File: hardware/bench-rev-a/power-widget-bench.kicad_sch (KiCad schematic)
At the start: 0 parts

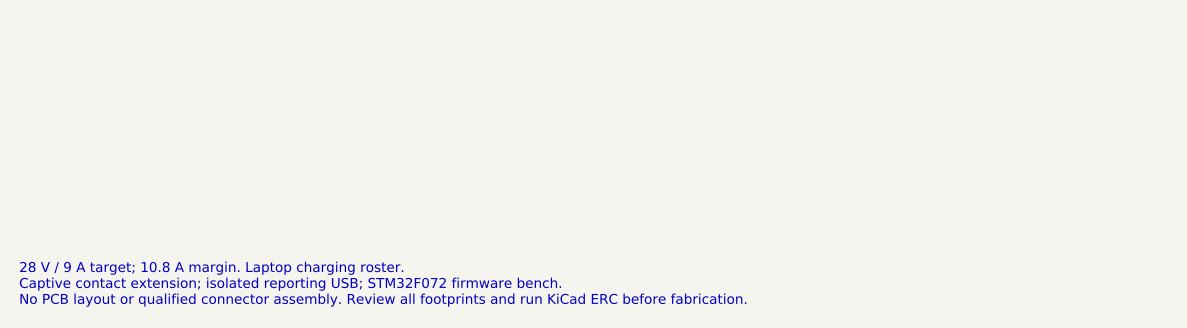
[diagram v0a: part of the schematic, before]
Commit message: Route the firmware bench PCB and record clean native KiCad checks
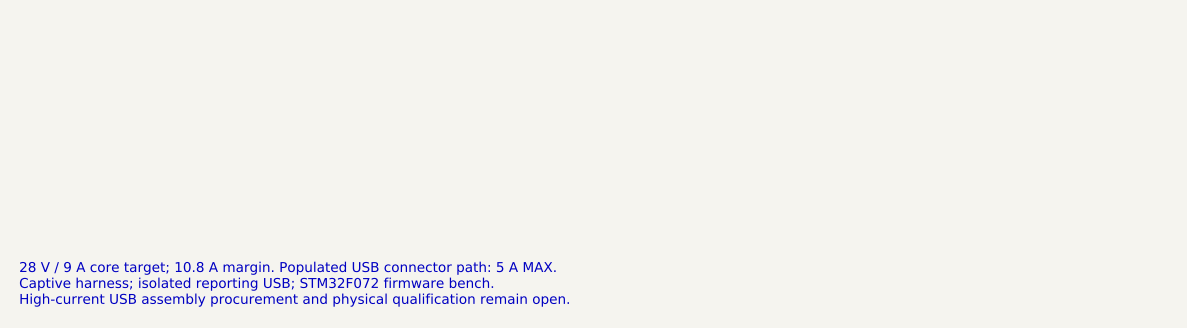
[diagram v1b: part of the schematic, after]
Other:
- note added: "28 V / 9 A core target; 10.8 A margin. Populated USB connector path: 5 A MAX. Captive harness; isolated reporting USB; STM32F072 firmware bench. High-current USB assembly procurement and physical qualification remain open."
- note removed: "28 V / 9 A target; 10.8 A margin. Laptop charging roster. Captive contact extension; isolated reporting USB; STM32F072 firmware bench. No PCB layout or qualified connector assembly. Review all footprints and run KiCad ERC before fabrication."
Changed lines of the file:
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@@
 (sheet (at 220 109) (size 155 36) (stroke (width 0.254) (type default)) (fill (color 0 0 0 0)) (property "Sheetname" "Reporting USB and MCU" (at 220 107 0) (effects (font (size 1.27 1.27)) (justify left))) (property "Sheetfile" "04-usb-mcu.kicad_sch" (at 220 147 0) (effects (font (size 1.0 1.0)) (justify left))) (instances (project "power-widget-bench" (path "/053fe491-f810-5db4-9f60-f0f5a50719e1" (page "5")))))
 (sheet (at 25 176) (size 155 36) (stroke (width 0.254) (type default)) (fill (color 0 0 0 0)) (property "Sheetname" "Firmware debug access" (at 25 174 0) (effects (font (size 1.27 1.27)) (justify left))) (property "Sheetfile" "05-debug.kicad_sch" (at 25 214 0) (effects (font (size 1.0 1.0)) (justify left))) (instances (project "power-widget-bench" (path "/053fe491-f810-5db4-9f60-f0f5a50719e1" (page "6")))))
-(text "28 V / 9 A target; 10.8 A margin. Laptop charging roster.
-Captive contact extension; isolated reporting USB; STM32F072 firmware bench.
-No PCB layout or qualified connector assembly. Review all footprints and run KiCad ERC before fabrication." (at 25 258 0) (effects (font (size 1.1 1.1)) (justify left)))
+(text "28 V / 9 A core target; 10.8 A margin. Populated USB connector path: 5 A MAX.\nCaptive harness; isolated reporting USB; STM32F072 firmware bench.\nHigh-current USB assembly procurement and physical qualification remain open." (at 25 258 0) (effects (font (size 1.1 1.1)) (justify left)))
 (sheet_instances (path "/" (page "1")))
 )

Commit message: Make single-sheet layout the canonical KiCad schematic and export README from it
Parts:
- added C1: 100nF 100V differential, PowerWidget:C_0805_2012Metric, symbol Bench:C_C1
- added C10: 1uF 10V at connector, PowerWidget:C_0805_2012Metric, symbol Bench:C_C10
- added C11: 100nF 10V at U3.24, PowerWidget:C_0805_2012Metric, symbol Bench:C_C11
- added C12: 100nF 10V at U3.48, PowerWidget:C_0805_2012Metric, symbol Bench:C_C12
- added C13: 100nF 10V at U3.36, PowerWidget:C_0805_2012Metric, symbol Bench:C_C13
- added C14: 100nF 10V at U3.1, PowerWidget:C_0805_2012Metric, symbol Bench:C_C14
- added C15: 100nF 10V at U3.9, PowerWidget:C_0805_2012Metric, symbol Bench:C_C15
- added C16: 1uF 10V, PowerWidget:C_0805_2012Metric, symbol Bench:C_C16
- added C17: 100nF reset, PowerWidget:C_0805_2012Metric, symbol Bench:C_C17
- added C18: 100nF 10V at U7.1, PowerWidget:C_0805_2012Metric, symbol Bench:C_C18
- added C19: 1uF 10V at U7.6, PowerWidget:C_0805_2012Metric, symbol Bench:C_C19
- added C2: 10nF 100V X7R, PowerWidget:C_0805_2012Metric, symbol Bench:C_C2
- added C20: 22uF 50V X7R MID, PowerWidget:C_1210_3225Metric, symbol Bench:C_C20
- added C21: 22uF 50V X7R MID, PowerWidget:C_1210_3225Metric, symbol Bench:C_C21
- added C3: 100nF 10V at U1, PowerWidget:C_0805_2012Metric, symbol Bench:C_C3
- added C4: 100nF 10V at U2.8, PowerWidget:C_0805_2012Metric, symbol Bench:C_C4
- added C5: 100nF 10V at U2.1, PowerWidget:C_0805_2012Metric, symbol Bench:C_C5
- added C6: 1uF 100V X7R, PowerWidget:C_1210_3225Metric, symbol Bench:C_C6
- added C7: 2u2 10V X7R, PowerWidget:C_0805_2012Metric, symbol Bench:C_C7
- added C8: 1uF 10V, PowerWidget:C_0805_2012Metric, symbol Bench:C_C8
- added C9: 4u7 10V, PowerWidget:C_0805_2012Metric, symbol Bench:C_C9
- added D1: Activity LED, PowerWidget:LED_0805_2012Metric, symbol Bench:C_D1
- added J1: USB4115-03-C / USB path 5A MAX, PowerWidget:USB_C_Receptacle_GCT_USB4115-03-C, symbol Bench:C_J1
- added J10: UART 3.3V logic, PowerWidget:PinHeader_1x04_P2.54mm_Vertical, symbol Bench:C_J10
- added J11: Spare GPIO / SPI, PowerWidget:PinHeader_1x08_P2.54mm_Vertical, symbol Bench:C_J11
- added J2: 691137710002 / force terminal, PowerWidget:Force_5mm_2pin, symbol Bench:C_J2
- added J3: 691137710002 / force terminal, PowerWidget:Force_5mm_2pin, symbol Bench:C_J3
- added J4: Kelvin probe pads; NOT force pins, PowerWidget:PinHeader_1x04_P2.54mm_Vertical, symbol Bench:C_J4
- added J5: PC I2C / external MCU, PowerWidget:PinHeader_1x04_P2.54mm_Vertical, symbol Bench:C_J5
- added J6: INLINE I2C debug, PowerWidget:PinHeader_1x04_P2.54mm_Vertical, symbol Bench:C_J6
- added J7: Floating external 3.3V, PowerWidget:PinHeader_1x02_P2.54mm_Vertical, symbol Bench:C_J7
- added J8: USB4105-GF-A-120 / reporting, PowerWidget:USB_C_Receptacle_GCT_USB4105-xx-A_16P_TopMnt_Horizontal, symbol Bench:C_J8
- added J9: Cortex SWD 2x5 1.27mm, PowerWidget:PinHeader_2x05_P1.27mm_Vertical, symbol Bench:C_J9
- added JP1: SENSOR SUPPLY: one shunt only, PowerWidget:PinHeader_1x03_P2.54mm_Vertical, symbol Bench:C_JP1
- added JP2: PC supply current link, PowerWidget:PinHeader_1x02_P2.54mm_Vertical, symbol Bench:C_JP2
- added JP3: INLINE self-current link, PowerWidget:PinHeader_1x02_P2.54mm_Vertical, symbol Bench:C_JP3
- added JP4: External-master enable; DNF, PowerWidget:PinHeader_1x02_P2.54mm_Vertical, symbol Bench:C_JP4
- added P1: Captive harness solder termination, PowerWidget:Captive_Termination, symbol Bench:C_P1
- added R1: WSK25125L000DEA / 5mR 1W, PowerWidget:WSK2512_5mR, symbol Bench:C_R1
- added R10: 10R 0.25W branch feed, PowerWidget:R_0805_2012Metric, symbol Bench:C_R10
- added R13: 5k1 1% Rd, PowerWidget:R_0805_2012Metric, symbol Bench:C_R13
- added R14: 5k1 1% Rd, PowerWidget:R_0805_2012Metric, symbol Bench:C_R14
- added R15: 0R tuning footprint, PowerWidget:R_0805_2012Metric, symbol Bench:C_R15
- added R16: 0R tuning footprint, PowerWidget:R_0805_2012Metric, symbol Bench:C_R16
- added R17: 10R VDDA filter, PowerWidget:R_0805_2012Metric, symbol Bench:C_R17
- added R18: 100k 1%, PowerWidget:R_0805_2012Metric, symbol Bench:C_R18
- added R19: 100k 1%, PowerWidget:R_0805_2012Metric, symbol Bench:C_R19
- added R2: 0R shield bond, PowerWidget:R_0805_2012Metric, symbol Bench:C_R2
- added R20: 0R PC shell bond, PowerWidget:R_0805_2012Metric, symbol Bench:C_R20
- added R21: 10k reset pull-up, PowerWidget:R_0805_2012Metric, symbol Bench:C_R21
- added R22: 10k boot pull-down, PowerWidget:R_0805_2012Metric, symbol Bench:C_R22
- added R23: 10k button pull-up, PowerWidget:R_0805_2012Metric, symbol Bench:C_R23
- added R24: 1k LED limiter, PowerWidget:R_0805_2012Metric, symbol Bench:C_R24
- added R25: 100k enable pull-down, PowerWidget:R_0805_2012Metric, symbol Bench:C_R25
- added R26: 10k override limiter, PowerWidget:R_0805_2012Metric, symbol Bench:C_R26
- added R3: 10R 0.1% matched, PowerWidget:R_0805_2012Metric, symbol Bench:C_R3
- added R4: 10R 0.1% matched, PowerWidget:R_0805_2012Metric, symbol Bench:C_R4
- added R5: 100R, PowerWidget:R_0805_2012Metric, symbol Bench:C_R5
- added R6: 2k2 pull-up, PowerWidget:R_0805_2012Metric, symbol Bench:C_R6
- added R7: 2k2 pull-up, PowerWidget:R_0805_2012Metric, symbol Bench:C_R7
- added R8: 2k2 pull-up, PowerWidget:R_0805_2012Metric, symbol Bench:C_R8
- added R9: 2k2 pull-up, PowerWidget:R_0805_2012Metric, symbol Bench:C_R9
- added SW1: RESET pushbutton, PowerWidget:SW_SPST_TL3342, symbol Bench:C_SW1
- added SW2: BOOT pushbutton, PowerWidget:SW_SPST_TL3342, symbol Bench:C_SW2
- added SW3: USER pushbutton, PowerWidget:SW_SPST_TL3342, symbol Bench:C_SW3
- added TP1: VBUS_A, PowerWidget:TestPoint_Pad_D2.0mm, symbol Bench:C_TP1
- added TP10: ALERT: floating scope only, PowerWidget:TestPoint_Pad_D2.0mm, symbol Bench:C_TP10
- added TP2: VBUS_B, PowerWidget:TestPoint_Pad_D2.0mm, symbol Bench:C_TP2
- added TP3: GND_INLINE, PowerWidget:TestPoint_Pad_D2.0mm, symbol Bench:C_TP3
- added TP4: CONTACT_A5, PowerWidget:TestPoint_Pad_D2.0mm, symbol Bench:C_TP4
- added TP5: CONTACT_B5, PowerWidget:TestPoint_Pad_D2.0mm, symbol Bench:C_TP5
- added TP6: INLINE_DP, PowerWidget:TestPoint_Pad_D2.0mm, symbol Bench:C_TP6
- added TP7: INLINE_DM, PowerWidget:TestPoint_Pad_D2.0mm, symbol Bench:C_TP7
- added TP8: CONTACT_A8, PowerWidget:TestPoint_Pad_D2.0mm, symbol Bench:C_TP8
- added TP9: CONTACT_B8, PowerWidget:TestPoint_Pad_D2.0mm, symbol Bench:C_TP9
- added U1: INA228AIDGSR, PowerWidget:VSSOP-10_3x3mm_P0.5mm, symbol Bench:C_U1
- added U2: ISO1641BD, PowerWidget:SOIC-8_3.9x4.9mm_P1.27mm, symbol Bench:C_U2
- added U3: STM32F072CBT6 / 128K flash, PowerWidget:LQFP-48_7x7mm_P0.5mm, symbol Bench:C_U3
- added U4: TPS7A4333DGQR, PowerWidget:HVSSOP10_DGQ, symbol Bench:C_U4
- added U5: TLV75533PDBVR, PowerWidget:SOT-23-5, symbol Bench:C_U5
- added U6: USBLC6-2SC6, PowerWidget:SOT-23-6, symbol Bench:C_U6
- added U7: TPS22919DCKR, PowerWidget:SOT-363_SC-70-6, symbol Bench:C_U7
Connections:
- new net 3V3_INLINE: C3.1, C4.1, J6.2, JP1.2, R8.2, R9.2, U1.6 (VS), U2.8 (VCC2)
- new net 3V3_INLINE_LDO: C7.1, JP1.1, U4.1 (OUT)
- new net 3V3_ISO_PC: C19.1, C5.1, J5.2, R6.2, R7.2, U2.1 (VCC1), U7.5 (QOD), U7.6 (VOUT)
- new net 3V3_PC: C11.1, C12.1, C13.1, C14.1, C18.1, C9.1, J10.4, J11.2, J9.1 (VTref), JP4.1, R17.1, R21.1, R23.1, SW2.2, U3.1 (VBAT), U3.24 (VDD), U3.36 (VDDIO2), U3.48 (VDD), U5.5 (OUT), U7.1 (IN)
- new net ALERT_INLINE: TP10.1, U1.3 (ALERT)
- new net BOOT0_PC: R22.1, SW2.1, U3.44 (BOOT0)
- new net BUTTON_PC: R23.2, SW3.1, U3.18 (PB0)
- new net CONTACT_A10: J1.A10, P1.A10
- new net CONTACT_A11: J1.A11, P1.A11
- new net CONTACT_A2: J1.A2, P1.A2
- new net CONTACT_A3: J1.A3, P1.A3
- new net CONTACT_A5: J1.A5, P1.A5, TP4.1
- new net CONTACT_A8: J1.A8, P1.A8, TP8.1
- new net CONTACT_B10: J1.B10, P1.B10
- new net CONTACT_B11: J1.B11, P1.B11
- new net CONTACT_B2: J1.B2, P1.B2
- new net CONTACT_B3: J1.B3, P1.B3
- new net CONTACT_B5: J1.B5, P1.B5, TP5.1
- new net CONTACT_B8: J1.B8, P1.B8, TP9.1
- new net EXT_3V3_INLINE: J7.1, JP1.3
- new net GND_INLINE: C2.2, C20.2, C21.2, C3.2, C4.2, C6.2, C7.2, J1.A1, J1.A12, J1.B1, J1.B12, J2.2, J3.2, J4.4, J6.1, J7.2, P1.A1, P1.A12, P1.B1, P1.B12, R2.2, TP3.1, U1.1 (A1), U1.2 (A0), U1.7 (GND), U2.5 (GND2), U4.11 (EP), U4.4 (MVSEL1), U4.5 (GND), U4.7 (MVSEL2)
- new net GND_PC: C10.2, C11.2, C12.2, C13.2, C14.2, C15.2, C16.2, C17.2, C18.2, C19.2, C5.2, C8.2, C9.2, D1.1 (K), J10.1, J11.1, J5.1, J8.A1, J8.A12, J8.B1, J8.B12, J9.3 (GND), J9.5 (GND), J9.9 (GNDDetect), R13.2, R14.2, R19.2, R20.2, R22.2, R25.2, SW1.2, SW3.2, U2.4 (GND1), U3.23 (VSS), U3.35 (VSS), U3.47 (VSS), U3.8 (VSSA), U5.2 (GND), U6.2 (GND), U7.2 (GND)
- new net GPIO_PA4: J11.3, U3.14 (PA4)
- new net GPIO_PA5: J11.4, U3.15 (PA5)
- new net GPIO_PA6: J11.5, U3.16 (PA6)
- new net GPIO_PA7: J11.6, U3.17 (PA7)
- new net GPIO_PB10: J11.7, U3.21 (PB10)
- new net GPIO_PB11: J11.8, U3.22 (PB11)
- new net INLINE_DM: J1.A7, J1.B7, P1.A7, TP7.1
- new net INLINE_DP: J1.A6, J1.B6, P1.A6, TP6.1
- new net INLINE_FEED: JP3.2, R10.1
- new net INLINE_LDO_IN: C6.1, R10.2, U4.10 (IN)
- new net INLINE_MID: C20.1, C21.1, U4.8 (MID_OUT)
- new net ISO_EN_PC: R25.1, R26.2, U3.11 (PA1), U7.3 (ON)
- new net ISO_FORCE_PC: JP4.2, R26.1
- new net LED_ANODE_PC: D1.2 (A), R24.2
- new net LED_PC: R24.1, U3.19 (PB1)
- new net NRST_PC: C17.1, J9.10 (nRESET), R21.2, SW1.1, U3.7 (NRST)
- new net PC_5V_LDO: C8.1, JP2.2, U5.1 (IN), U5.3 (EN)
- new net PC_CC1: J8.A5, R13.1
- new net PC_CC2: J8.B5, R14.1
- new net PC_DM_CONN: J8.A7, J8.B7, R16.1, U6.3 (IO2), U6.4 (IO2)
- new net PC_DP_CONN: J8.A6, J8.B6, R15.1, U6.1 (IO1), U6.6 (IO1)
- new net PC_VBUS_DETECT: R18.2, R19.1, U3.10 (PA0)
- new net SCL_INLINE: J6.3, R9.1, U1.5 (SCL), U2.6 (SCL2)
- new net SCL_PC: J5.3, R7.1, U2.3 (SCL1), U3.42 (PB6)
- new net SDA_INLINE: J6.4, R8.1, U1.4 (SDA), U2.7 (SDA2)
- new net SDA_PC: J5.4, R6.1, U2.2 (SDA1), U3.43 (PB7)
- new net SHIELD_INLINE: J1.S (SHIELD), P1.S (SHIELD), R2.1
- new net SHIELD_PC: J8.S (SHIELD), R20.1
- new net SHUNT_MINUS: C1.2, R4.2, U1.9 (IN-)
- new net SHUNT_PLUS: C1.1, R3.2, U1.10 (IN+)
- new net SHUNT_SA: J4.1, R1.3 (E1), R3.1
- new net SHUNT_SB: J4.2, R1.4 (E2), R4.1
- new net SWCLK_PC: J9.4 (SWCLK), U3.37 (PA14)
- new net SWDIO_PC: J9.2 (SWDIO), U3.34 (PA13)
- new net UART_RX_PC: J10.3, U3.13 (PA3)
- new net UART_TX_PC: J10.2, U3.12 (PA2)
- new net USB_DM_MCU: R16.2, U3.32 (PA11)
- new net USB_DP_MCU: R15.2, U3.33 (PA12)
- new net VBUS_A: J1.A4, J1.A9, J1.B4, J1.B9, J2.1, JP3.1, R1.1 (I1), TP1.1
- new net VBUS_B: J3.1, J4.3, P1.A4, P1.A9, P1.B4, P1.B9, R1.2 (I2), R5.1, TP2.1
- new net VBUS_FILTER: C2.1, R5.2, U1.8 (VBUS)
- new net VBUS_PC: C10.1, J8.A4, J8.A9, J8.B4, J8.B9, JP2.1, R18.1, U6.5 (VBUS)
- new net VDDA_PC: C15.1, C16.1, R17.2, U3.9 (VDDA)
- no-connect marks 0 -> 30
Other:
- removed sheet Firmware debug access
- removed sheet Inline path
- removed sheet Local supplies
- removed sheet Reporting USB and MCU
- removed sheet Sensing and isolation
- note added: "01 THROUGH POWER"
- note added: "02 MEASUREMENT"
- note added: "03 INLINE SUPPLY"
- note added: "04 ISOLATED I²C"
- note added: "05 REPORTING USB"
- note added: "06 ACQUISITION + FIRMWARE"
- note added: "07 PC SUPPLY + SUSPEND"
- note added: "28 V / 9 A target; selected USB population: 5 A MAX"
- note added: "BENCH REVISION A / CANONICAL SINGLE-SHEET SCHEMATIC"
- note added: "Canonical source: power-widget-bench.kicad_sch. Previews exported directly by kicad-cli."
- note added: "Dot = junction. Undotted crossing = no connection. Comma-separated pins share a net. Cross = deliberately unconnected pin."
- note added: "Each contact appears once."
- note added: "Each physical component appears once. Both grounds remain separate. Engineering draft; not qualified hardware."
- note added: "Edit the native schematic. Do not rebuild it from a documentation diagram."
- note added: "FOUR-TERMINAL SHUNT"
- note added: "Follow both sense wires"
- note added: "Force pins carry the load."
- note added: "INLINE | ISOLATED PC"
- note added: "J1: charger / P1: device"
- note added: "JP1: ONE shunt, 1-2 normal / 2-3 external. JP2 and JP3 fitted. JP4 not fitted."
- note added: "Kelvin current + output voltage"
- note added: "Kelvin pins sense the drop."
- note added: "NATIVE KiCad / 82 physical components / 65 named nets / one sheet"
- note added: "ONE COMPLETE PATH"
- note added: "Only VBUS crosses R1."
- note added: "Other contacts pass through."
- note added: "POWER WIDGET"
- note added: "Taken upstream of the shunt"
- note added: "to the INA228 inputs."
- note removed: "28 V / 9 A core target; 10.8 A margin. Populated USB connector path: 5 A MAX. Captive harness; isolated reporting USB; STM32F072 firmware bench. High-current USB assembly procurement and physical qualification remain open."
- company: (none) -> Power Widget
- title: Power Widget bench prototype -> Power Widget - canonical single-sheet schematic
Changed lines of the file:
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@@
-(kicad_sch (version 20231120) (generator "power_widget") (paper "A3")
-(title_block (title "Power Widget bench prototype") (date "2026-09-10") (rev "A-DRAFT") (comment 1 "NOT FOR FABRICATION"))
-(sheet (at 25 42) (size 155 36) (stroke (width 0.254) (type default)) (fill (color 0 0 0 0)) (property "Sheetname" "Inline path" (at 25 40 0) (effects (font (size 1.27 1.27)) (justify left))) (property "Sheetfile" "01-inline.kicad_sch" (at 25 80 0) (effects (font (size 1.0 1.0)) (justify left))) (instances (project "power-widget-bench" (path "/053fe491-f810-5db4-9f60-f0f5a50719e1" (page "2")))))
-(sheet (at 220 42) (size 155 36) (stroke (width 0.254) (type default)) (fill (color 0 0 0 0)) (property "Sheetname" "Sensing and isolation" (at 220 40 0) (effects (font (size 1.27 1.27)) (justify left))) (property "Sheetfile" "02-sensing.kicad_sch" (at 220 80 0) (effects (font (size 1.0 1.0)) (justify left))) (instances (project "power-widget-bench" (path "/053fe491-f810-5db4-9f60-f0f5a50719e1" (page "3")))))
-(sheet (at 25 109) (size 155 36) (stroke (width 0.254) (type default)) (fill (color 0 0 0 0)) (property "Sheetname" "Local supplies" (at 25 107 0) (effects (font (size 1.27 1.27)) (justify left))) (property "Sheetfile" "03-supplies.kicad_sch" (at 25 147 0) (effects (font (size 1.0 1.0)) (justify left))) (instances (project "power-widget-bench" (path "/053fe491-f810-5db4-9f60-f0f5a50719e1" (page "4")))))
-(sheet (at 220 109) (size 155 36) (stroke (width 0.254) (type default)) (fill (color 0 0 0 0)) (property "Sheetname" "Reporting USB and MCU" (at 220 107 0) (effects (font (size 1.27 1.27)) (justify left))) (property "Sheetfile" "04-usb-mcu.kicad_sch" (at 220 147 0) (effects (font (size 1.0 1.0)) (justify left))) (instances (project "power-widget-bench" (path "/053fe491-f810-5db4-9f60-f0f5a50719e1" (page "5")))))
-(sheet (at 25 176) (size 155 36) (stroke (width 0.254) (type default)) (fill (color 0 0 0 0)) (property "Sheetname" "Firmware debug access" (at 25 174 0) (effects (font (size 1.27 1.27)) (justify left))) (property "Sheetfile" "05-debug.kicad_sch" (at 25 214 0) (effects (font (size 1.0 1.0)) (justify left))) (instances (project "power-widget-bench" (path "/053fe491-f810-5db4-9f60-f0f5a50719e1" (page "6")))))
-(text "28 V / 9 A core target; 10.8 A margin. Populated USB connector path: 5 A MAX.\nCaptive harness; isolated reporting USB; STM32F072 firmware bench.\nHigh-current USB assembly procurement and physical qualification remain open." (at 25 258 0) (effects (font (size 1.1 1.1)) (justify left)))
-(sheet_instances (path "/" (page "1")))
-)
